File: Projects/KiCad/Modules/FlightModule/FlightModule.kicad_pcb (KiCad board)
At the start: 2 copper layers, 110 x 95 mm, 66 parts, among them J1 Conn_01x08, J2 Conn_01x02_Pin, J3 Conn_01x02_Pin, J4 Conn_01x02_Pin, J5 Conn_01x02_Pin, J6 Conn_01x02_Pin, Q1 DTC143E, SW1 SW_DIP_x02, U1 MCP2562-E-P, U2 NUCLEO-F303K8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

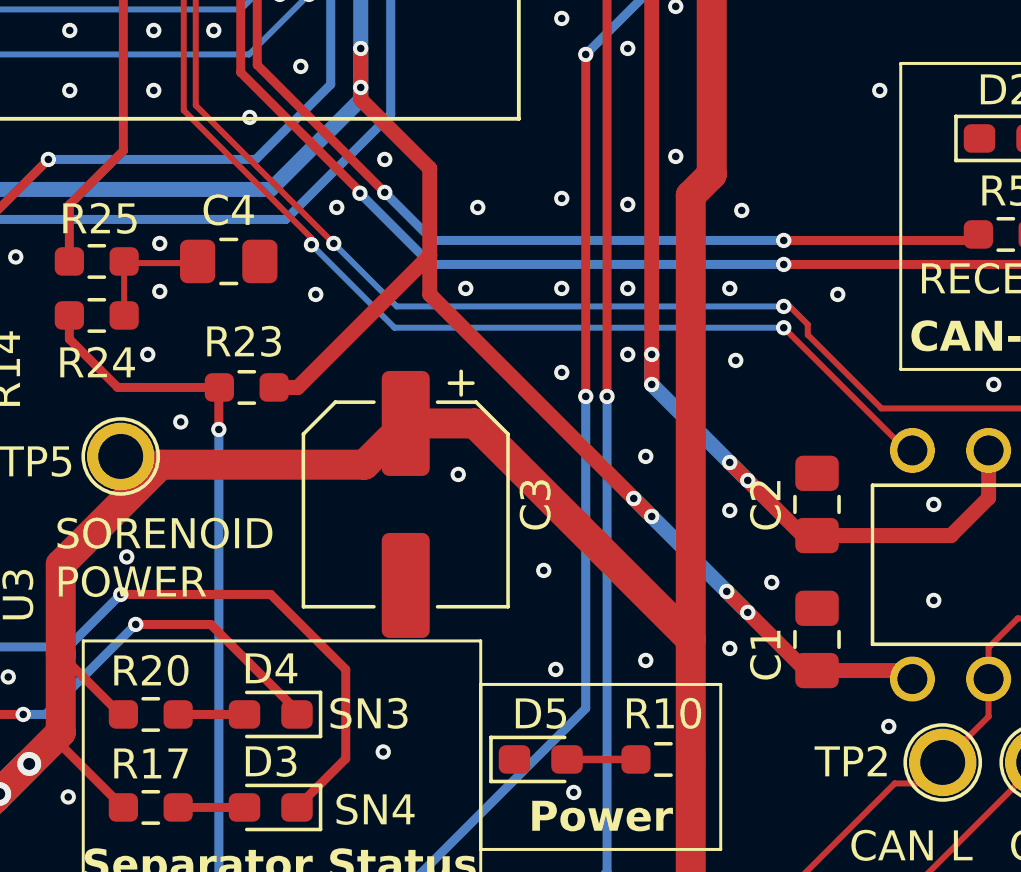
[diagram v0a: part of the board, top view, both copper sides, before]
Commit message: チップ積層セラミックコンデンサをSMD1608に変更
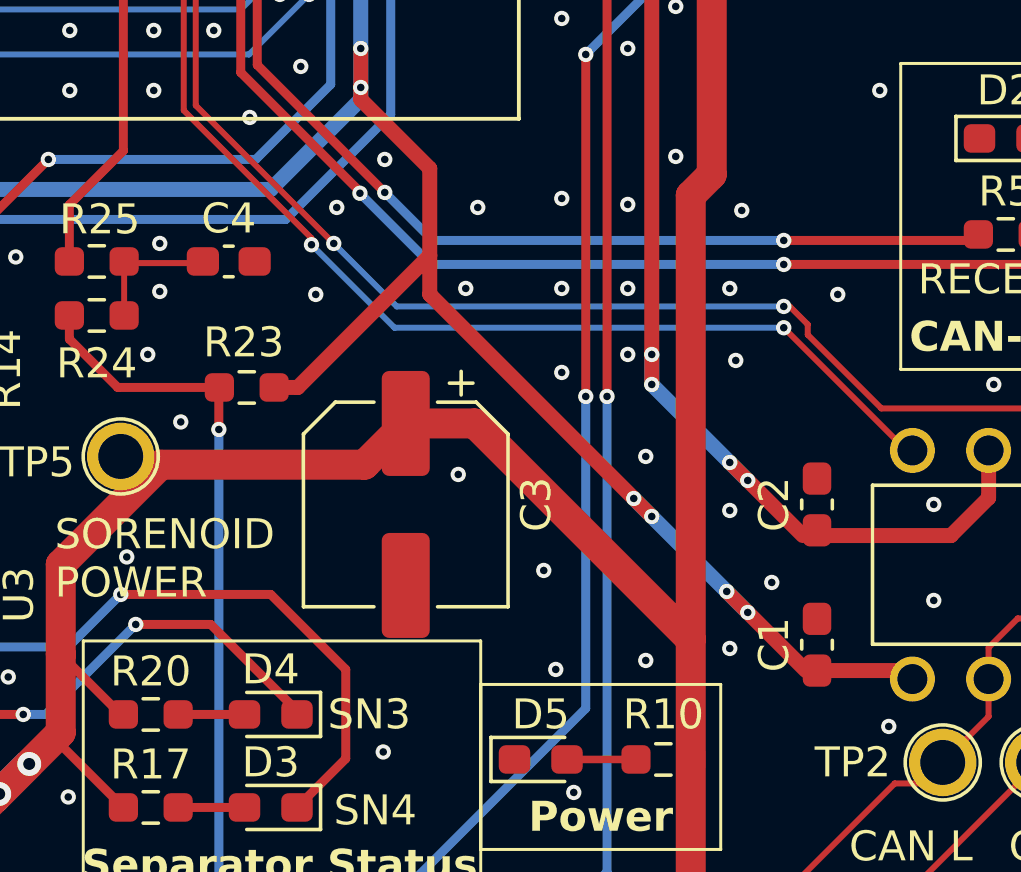
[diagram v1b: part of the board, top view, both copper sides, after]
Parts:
- C1, C2, C4: footprint Capacitor_SMD:C_0805_2012Metric_Pad1.18x1.45mm_HandSolder -> Capacitor_SMD:C_0603_1608Metric_Pad1.08x0.95mm_HandSolder
- moved C1 0.18 mm to (167.7, 120.7)

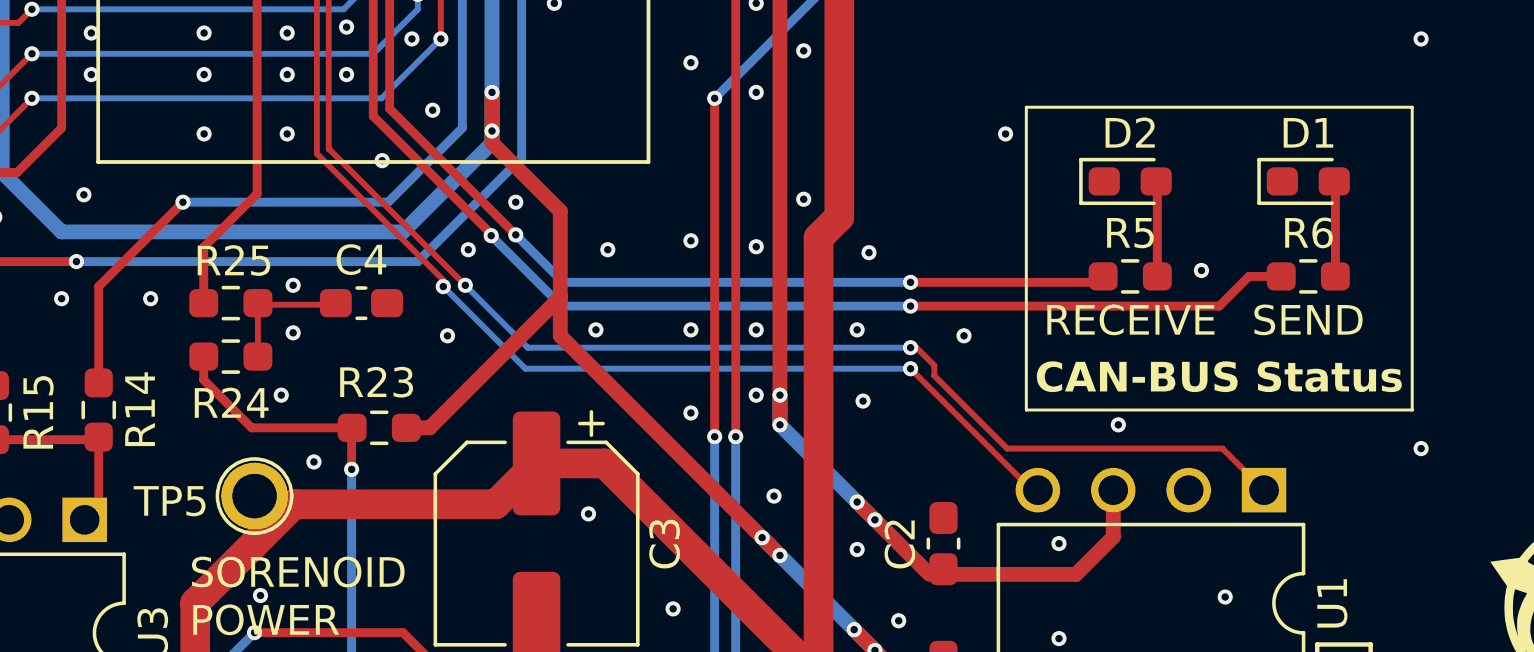
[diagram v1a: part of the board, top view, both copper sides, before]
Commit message: 抵抗の在庫に合わせてサイズを変更
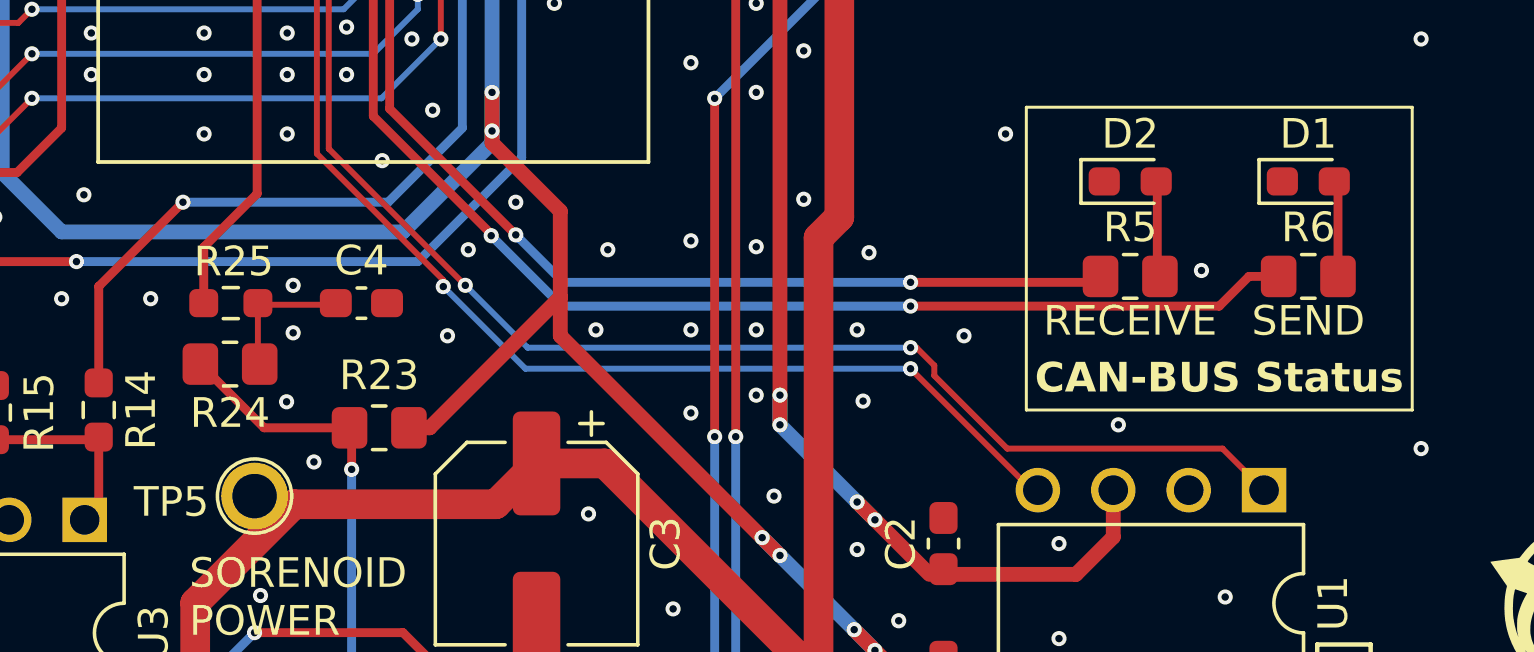
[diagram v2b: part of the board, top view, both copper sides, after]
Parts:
- R23, R24, R5, R6: footprint Resistor_SMD:R_0603_1608Metric_Pad0.98x0.95mm_HandSolder -> Resistor_SMD:R_0805_2012Metric_Pad1.20x1.40mm_HandSolder
- moved R24 0.25 mm to (143.7, 110.0)

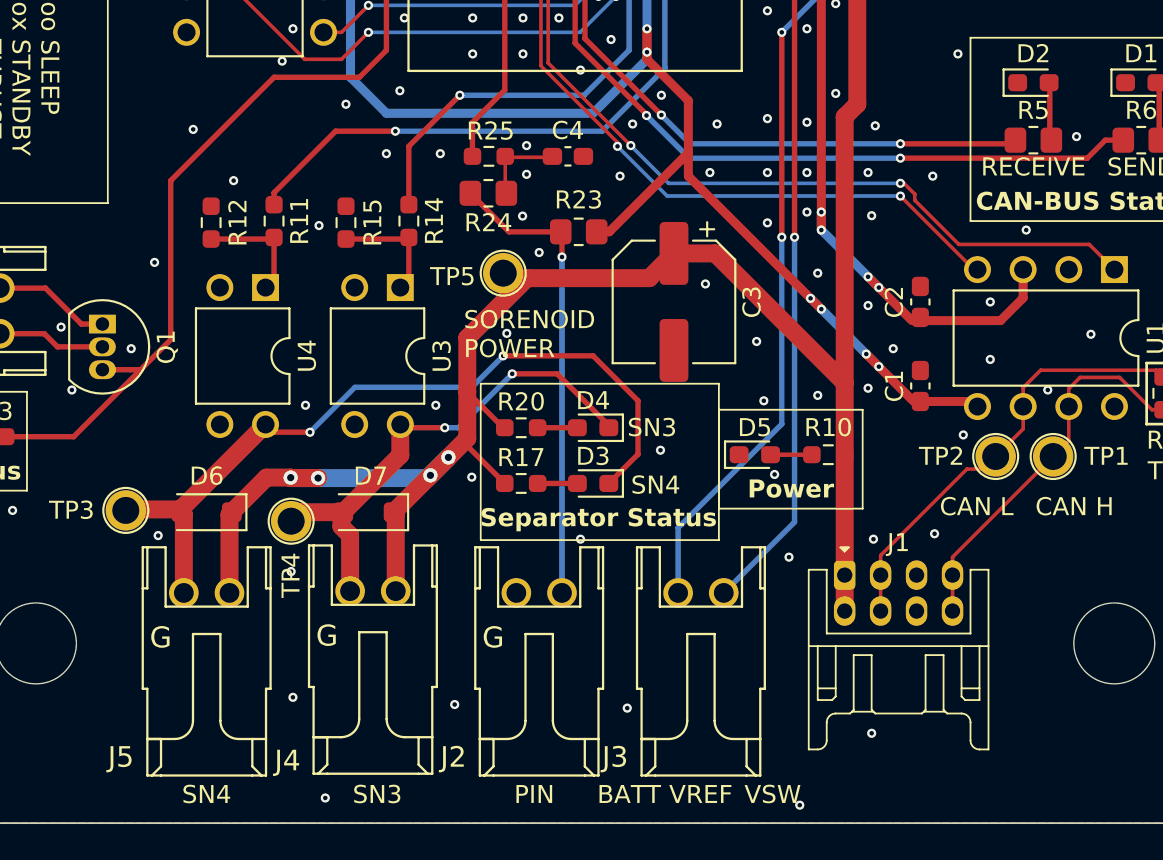
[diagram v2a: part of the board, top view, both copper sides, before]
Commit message: コネクタ位置を揃えた
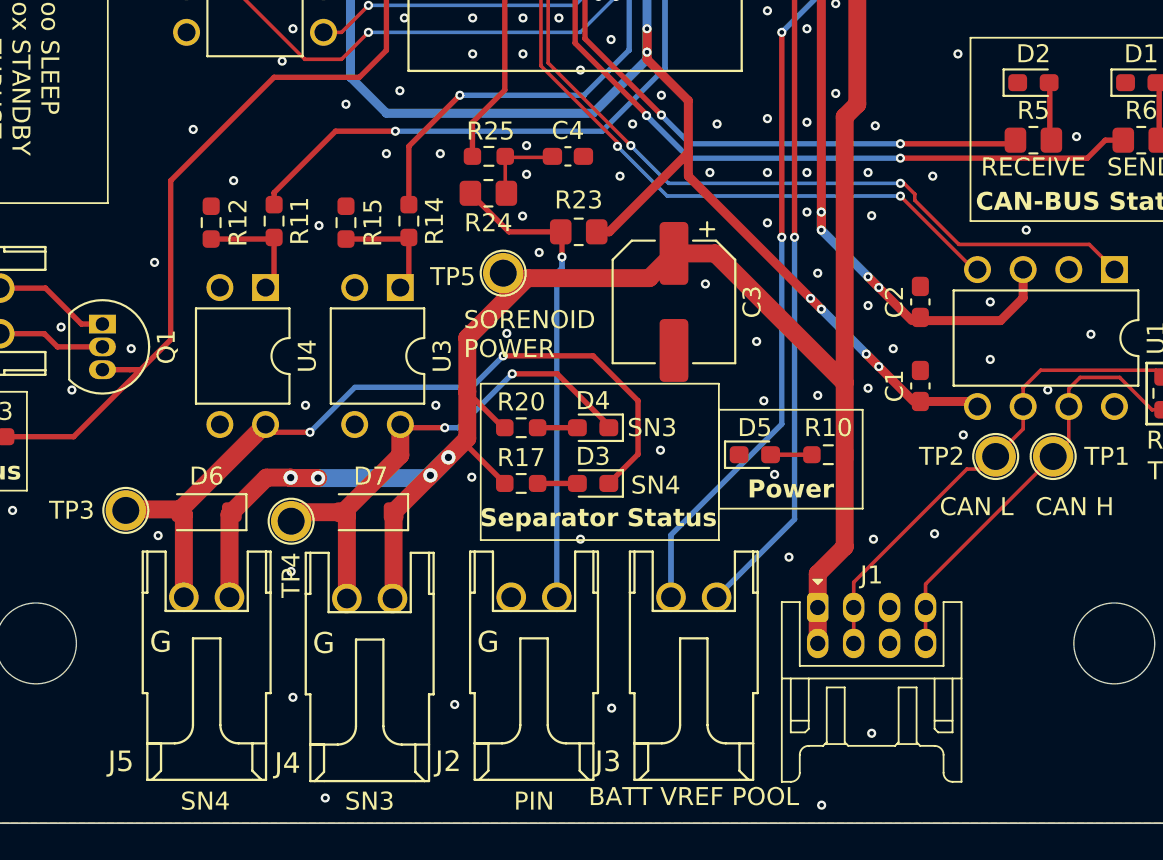
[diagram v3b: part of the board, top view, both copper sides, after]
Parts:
- moved J1 2.34 mm to (162.0, 133.0)
- moved J3 0.46 mm to (155.1, 136.2)
- moved J4 0.45 mm to (135.8, 132.5)
- moved J2 0.37 mm to (146.2, 136.2)
- moved J5 0.24 mm to (128.0, 136.2)
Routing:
- net SOLENOID_POWER: track 157.3 -> 160.1 mm
- net CAN_H: track 21.3 -> 23.7 mm
- net CAN_L: track 24.6 -> 27.0 mm
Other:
- board text added: "BATT VREF POOL"
- board text removed: "BATT"
- board text removed: "VREF"
- board text removed: "VSW"

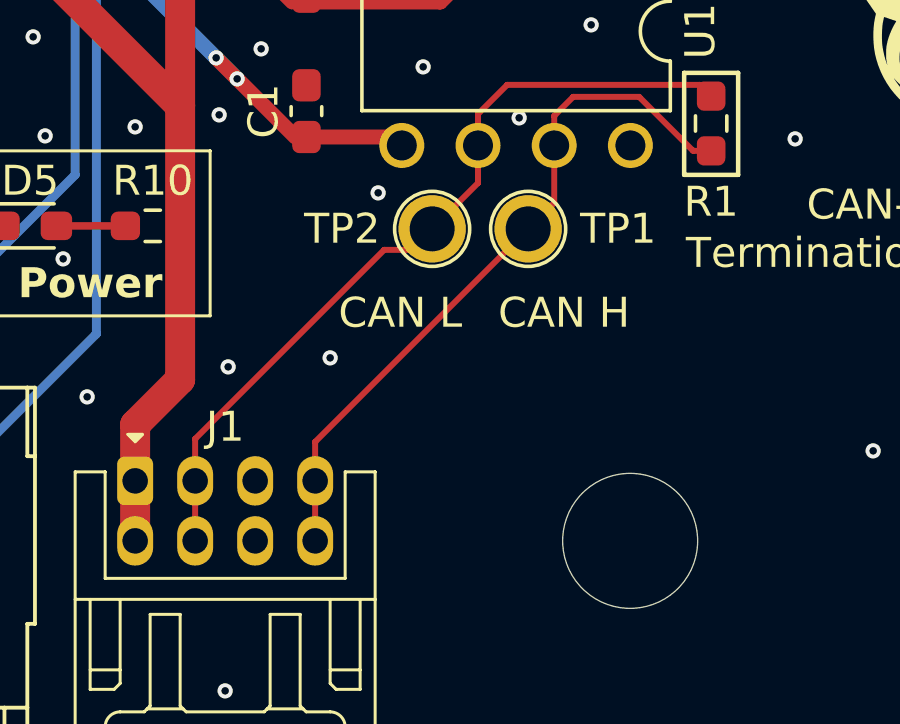
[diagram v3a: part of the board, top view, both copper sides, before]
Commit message: コネクタのピン配置を変更
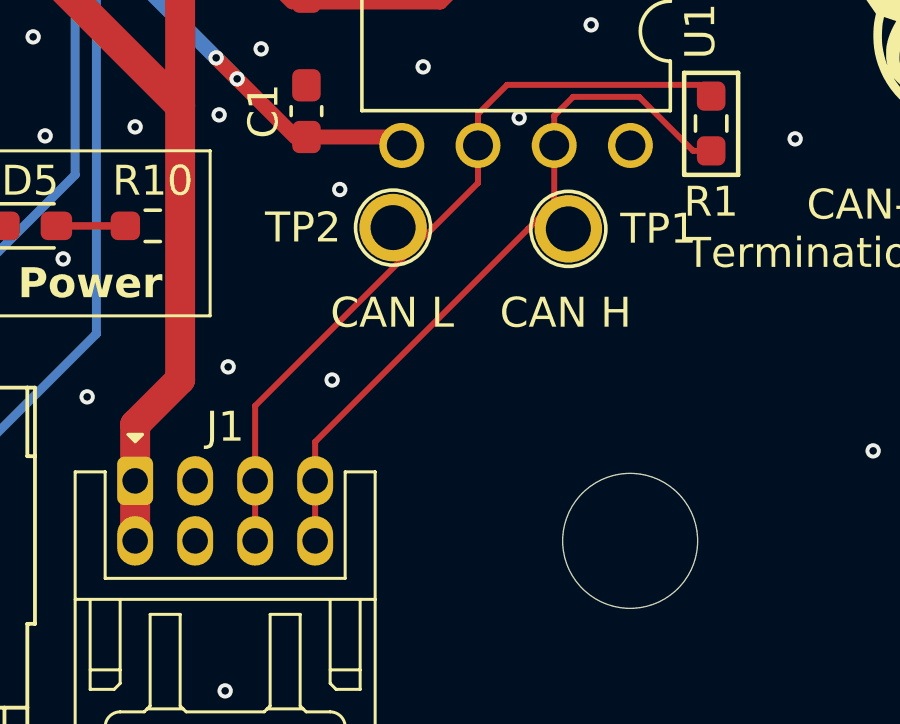
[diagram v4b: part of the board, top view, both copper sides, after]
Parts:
- moved TP1 1.34 mm to (176.4, 124.6)
- moved TP2 1.30 mm to (170.6, 124.6)
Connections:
- J1 pad 3: CAN_L -> GND
- J1 pad 4: CAN_L -> GND
- J1 pad 5: GND -> CAN_L
- J1 pad 6: GND -> CAN_L
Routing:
- net CAN_L: track 27.0 -> 25.6 mm

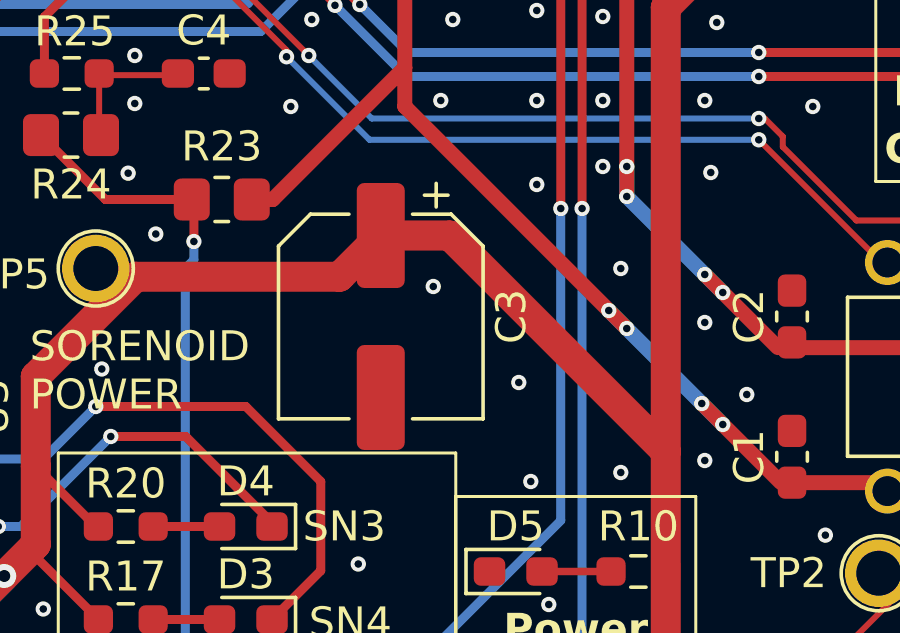
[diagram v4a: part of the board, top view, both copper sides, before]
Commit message: バッファコンデンサを表面実装に変更
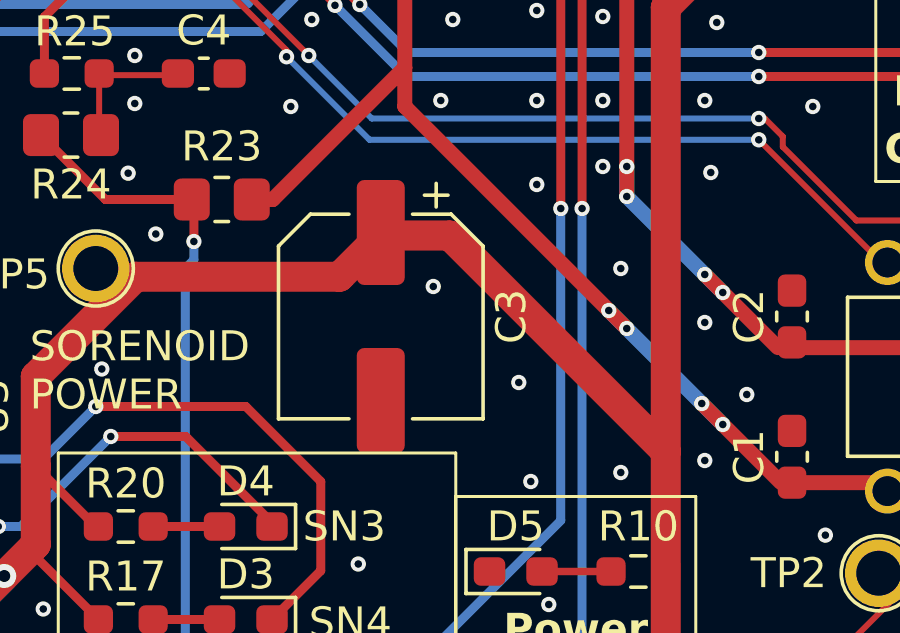
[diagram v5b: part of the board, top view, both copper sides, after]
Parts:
- C3: value 100μF -> 47μF; footprint Capacitor_SMD:CP_Elec_6.3x7.7 -> Capacitor_SMD:CP_Elec_6.3x5.9

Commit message: チェックよし（多分）
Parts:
- removed the G*** at (189.5, 101.4)
- added R26: 4.7kΩ, Resistor_SMD:R_0603_1608Metric_Pad0.98x0.95mm_HandSolder, F.Cu at (124.6, 114.3)
- added R27: 4.7kΩ, Resistor_SMD:R_0603_1608Metric_Pad0.98x0.95mm_HandSolder, F.Cu at (122.6, 114.3)
- Q1: value DTC143E -> Q_NPN_BEC; footprint Package_TO_SOT_THT:TO-92_Inline -> Package_TO_SOT_SMD:SC-59_Handsoldering
- moved Q1 2.44 mm to (123.6, 119.2)
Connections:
- Q1 pad 1: Net-(J6-Pin_1) -> Net-(Q1-B)
- Q1 pad 2: Net-(J6-Pin_2) -> Net-(J6-Pin_1)
- Q1 pad 3: CONTROL_CAMERA -> Net-(J6-Pin_2)
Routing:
- net Net-(Q1-B): track 0.00 -> 4.43 mm
- net Net-(J6-Pin_1): track 6.54 -> 10.0 mm
- net Net-(J6-Pin_2): track 6.02 -> 8.41 mm
- net CONTROL_CAMERA: track 53.5 -> 55.4 mm
